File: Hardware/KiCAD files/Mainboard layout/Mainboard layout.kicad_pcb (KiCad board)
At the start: 2 copper layers, 87 parts, among them J1 Conn_01x02, J10 Conn_01x02, J14 Conn_01x03, J15 Conn_01x03, J2 Conn_01x06, J28 Conn_01x03, J3 Conn_01x02, J31 JST_03, J33 Conn_01x04, J34 JST_03, J35 JST_03, J36 JST_03, J37 JST_03, J38 JST_03, J39 JST_03, J4 Conn_01x06, J5 Conn_01x04, J6 Conn_01x06, J7 Conn_01x06, J8 Conn_01x06, J9 Conn_01x10, Q2 2DD1664, Q4 2N7000, SW8 Push_Button, SW9 Push_Button, U12 ESP32-S3-WROOM-1, U3 PCA9534PW

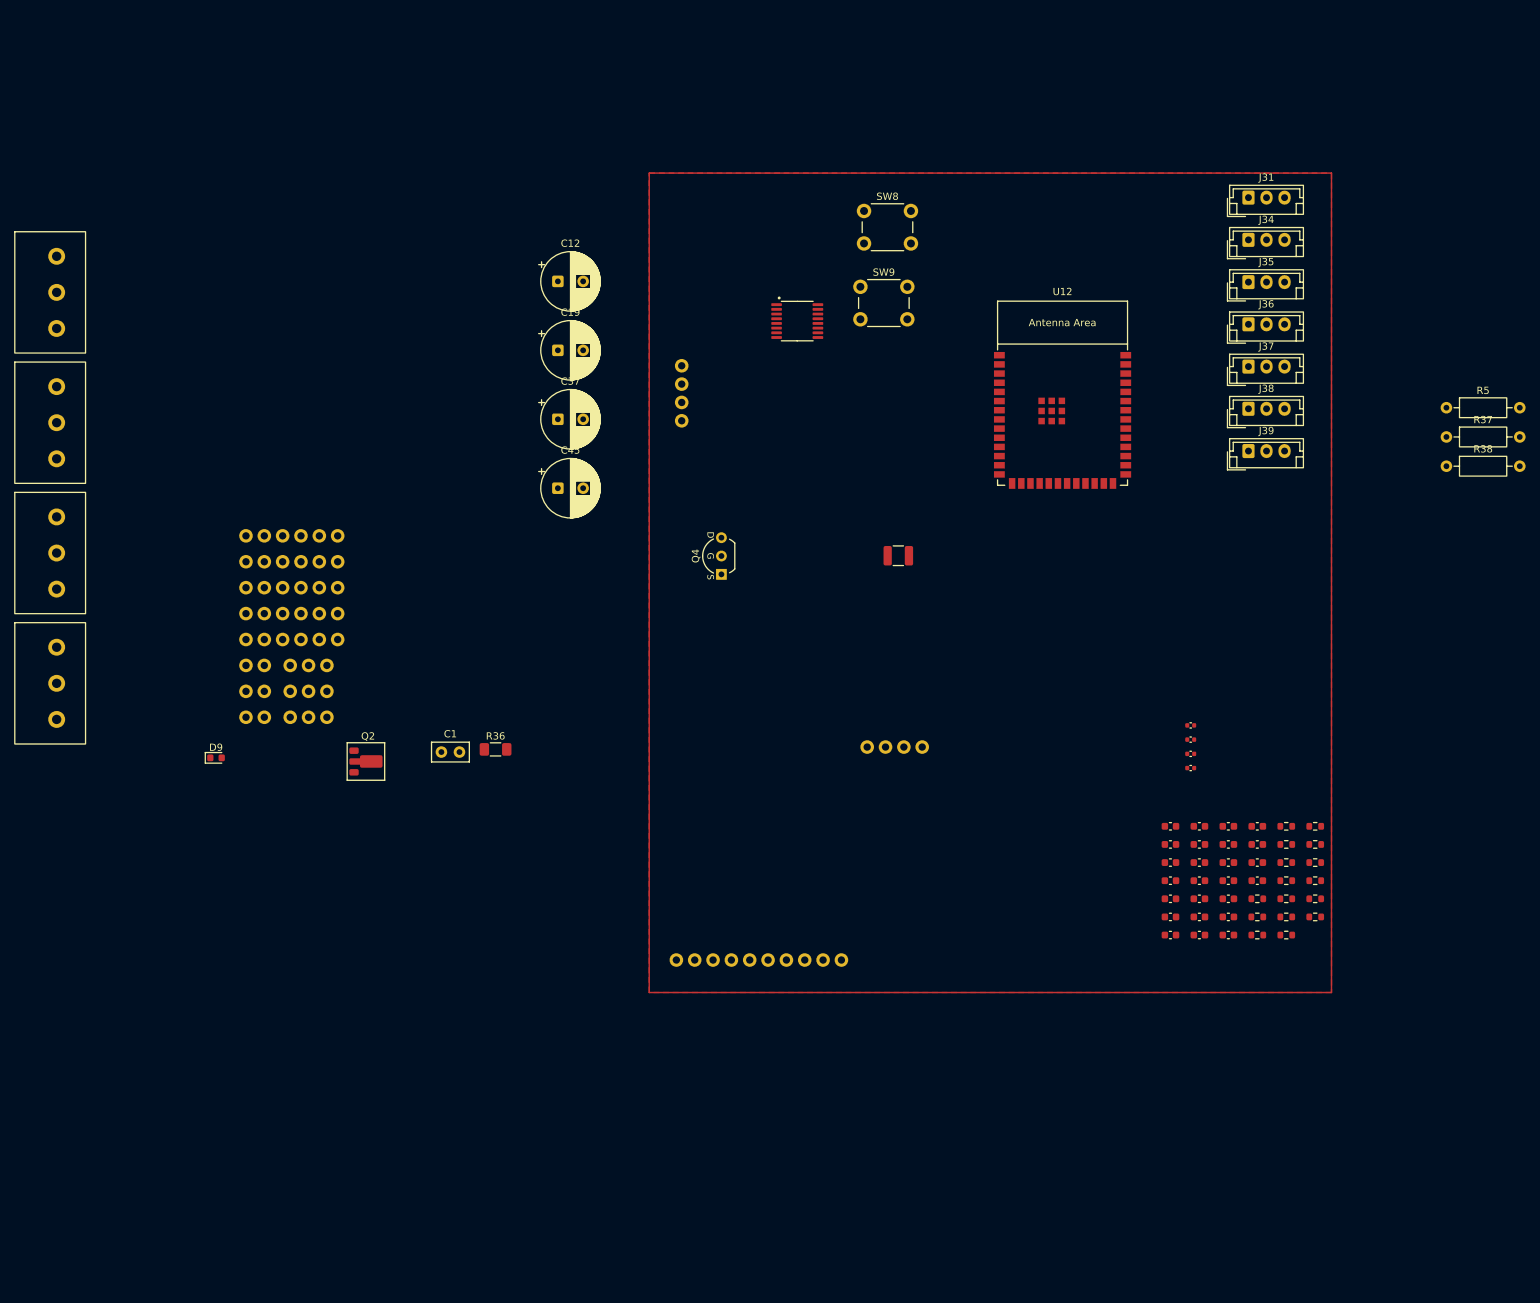
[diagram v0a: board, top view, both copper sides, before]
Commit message: Mainboard Layout V1
completed Mainboard V1 layout and one swapping side, a hotfix to come of the other board to take swapping side
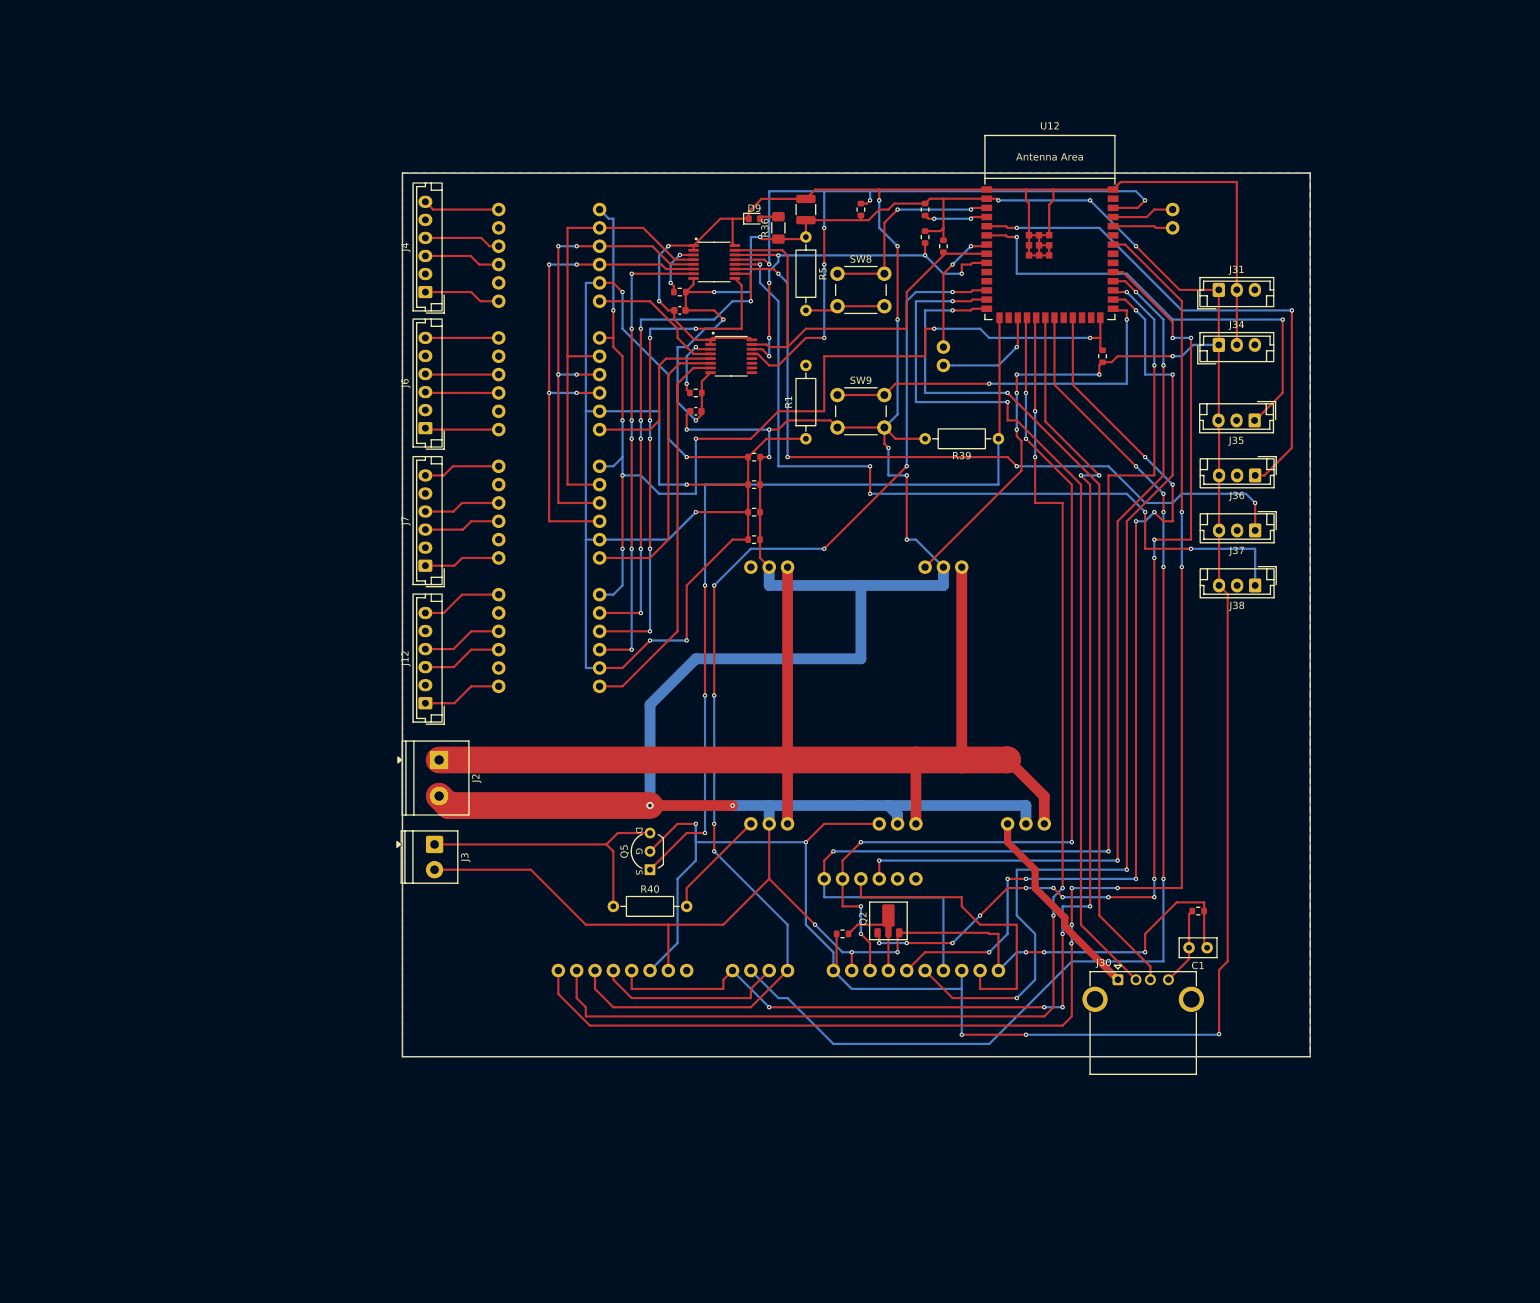
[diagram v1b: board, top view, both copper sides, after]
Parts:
- removed C10, C11, C13, C14, C15, C22, C29, C31, C32, C35, C36, C39, C40, C43, C44, C9: 0.1uF, PCM_SparkFun-Capacitor:C_0603_1608Metric
- removed C12, C19, C37, C45: 100uF_50V, Capacitor_THT:CP_Radial_D8.0mm_P3.50mm
- removed C17, C18, C30, C38: 4.7uF, PCM_SparkFun-Capacitor:C_0603_1608Metric
- removed C20, C27, C33, C41: 470nF, PCM_SparkFun-Capacitor:C_0402_1005Metric
- removed C21, C28, C34, C42: 10nF, PCM_SparkFun-Capacitor:C_0603_1608Metric
- removed J33: Conn_01x04, PCM_SparkFun-Connector:1x04_P2.54mm
- removed J39: JST_03, Connector_JST:JST_EH_B3B-EH-A_1x03_P2.50mm_Vertical
- removed Q4: 2N7000, PCM_Package_TO_SOT_THT_AKL:TO-92_Inline_Wide_SGD
- removed R10, R19, R24, R29: 1.5k, PCM_SparkFun-Resistor:R_0603_1608Metric
- removed R11, R21, R26, R31: 10k Linear, PCM_SparkFun-Resistor:Bourns-PDB18
- removed R12, R22, R27, R32: 10k, PCM_SparkFun-Resistor:R_0603_1608Metric
- removed R37, R38: 10k, Resistor_THT:R_Axial_DIN0207_L6.3mm_D2.5mm_P10.16mm_Horizontal
- added C23: 0.1uF, PCM_SparkFun-Capacitor:C_0603_1608Metric, F.Cu at (124.5, 47.0)
- added J11: Conn_01x06, PCM_SparkFun-Connector:1x06_P2.54mm, F.Cu at (97.2, 31.8)
- added J12: JST_06, Connector_JST:JST_EH_B6B-EH-A_1x06_P2.50mm_Vertical, F.Cu at (87.0, 87.4)
- added J13: Conn_01x08, PCM_SparkFun-Connector:1x08_P2.54mm, F.Cu at (123.2, 124.5)
- added J17: Conn_01x06, PCM_SparkFun-Connector:1x06_P2.54mm, F.Cu at (97.2, 49.5)
- added J19: Conn_01x06, PCM_SparkFun-Connector:1x06_P2.54mm, F.Cu at (97.2, 67.3)
- added J21: Conn_01x06, PCM_SparkFun-Connector:1x06_P2.54mm, F.Cu at (97.2, 85.1)
- added J22: Conn_01x03, PCM_SparkFun-Connector:1x03_P2.54mm, F.Cu at (156.2, 68.6)
- added J23: Conn_01x06, PCM_SparkFun-Connector:1x06_P2.54mm, F.Cu at (111.1, 31.8)
- added J24: Conn_01x06, PCM_SparkFun-Connector:1x06_P2.54mm, F.Cu at (111.1, 49.5)
- added J25: Conn_01x06, PCM_SparkFun-Connector:1x06_P2.54mm, F.Cu at (111.1, 67.3)
- added J26: Conn_01x06, PCM_SparkFun-Connector:1x06_P2.54mm, F.Cu at (111.1, 85.1)
- added J29: Conn_01x03, PCM_SparkFun-Connector:1x03_P2.54mm, F.Cu at (132.1, 68.6)
- added J30: USB-A1VSB6, Connector_USB:USB_A_Kycon_KUSBX-AS1N-B_Horizontal, F.Cu at (182.9, 125.7)
- added Q5: 2N7000, PCM_Package_TO_SOT_THT_AKL:TO-92_Inline_Wide_SGD, F.Cu at (118.1, 110.5)
- added R1: 1k, Resistor_THT:R_Axial_DIN0207_L6.3mm_D2.5mm_P10.16mm_Horizontal, F.Cu at (139.7, 50.8)
- added R107: 4K7, PCM_SparkFun-Resistor:R_0603_1608Metric, F.Cu at (132.5, 64.8)
- added R39: 10k, Resistor_THT:R_Axial_DIN0207_L6.3mm_D2.5mm_P10.16mm_Horizontal, F.Cu at (166.4, 50.8)
- added R40: 100k, Resistor_THT:R_Axial_DIN0207_L6.3mm_D2.5mm_P10.16mm_Horizontal, F.Cu at (113.0, 115.6)
- added R54: 10k, PCM_SparkFun-Resistor:R_0603_1608Metric, F.Cu at (124.5, 44.5)
- added R89: 4K7, PCM_SparkFun-Resistor:R_0603_1608Metric, F.Cu at (132.5, 53.3)
- added R90: 4K7, PCM_SparkFun-Resistor:R_0603_1608Metric, F.Cu at (132.5, 57.1)
- added R91: 4K7, PCM_SparkFun-Resistor:R_0603_1608Metric, F.Cu at (132.5, 61.0)
- added U5: PCA9534PW, PCM_SparkFun-Semiconductor-Standard:TSSOP-16_4.4x5mm_P0.65mm, F.Cu at (129.4, 39.4)
- J1: value Conn_01x02 -> Programmer pins Conn_01x02
- J2: value Conn_01x06 -> Screw_Terminal_2_P5.00mm; footprint PCM_SparkFun-Connector:1x06_P2.54mm -> TerminalBlock_Phoenix:TerminalBlock_Phoenix_PT-1,5-2-5.0-H_1x02_P5.00mm_Horizontal
- J3: value Conn_01x02 -> Screw_Terminal_2_P3.50mm; footprint PCM_SparkFun-Connector:1x02_P2.54mm -> TerminalBlock_Phoenix:TerminalBlock_Phoenix_PT-1,5-2-3.5-H_1x02_P3.50mm_Horizontal
- J4, J6, J7: value Conn_01x06 -> JST_06; footprint PCM_SparkFun-Connector:1x06_P2.54mm -> Connector_JST:JST_EH_B6B-EH-A_1x06_P2.50mm_Vertical
- moved J1 143.0 mm to (190.5, 19.1), turned to -90 degrees
- moved R51 118.3 mm to (122.2, 30.5), turned to 180 degrees
- moved R55 116.4 mm to (147.3, 19.1), turned to 90 degrees
- moved C16 110.0 mm to (122.2, 33.0), turned to 180 degrees
- moved C1 109.5 mm to (195.3, 121.3), turned to 180 degrees
- moved J10 109.4 mm to (158.8, 38.1), turned to -90 degrees
- moved D9 105.5 mm to (132.6, 20.3)
- moved R52 104.2 mm to (156.2, 22.9), turned to 90 degrees
- moved R53 104.0 mm to (158.8, 24.1), turned to 90 degrees
- moved R50 103.2 mm to (156.2, 19.1), turned to 90 degrees
- moved J28 100.5 mm to (167.6, 104.1)
- moved R5 91.8 mm to (139.7, 22.9), turned to -90 degrees
- moved J8 86.7 mm to (142.2, 111.8)
- moved J15 83.6 mm to (149.9, 104.1)
- moved R36 82.2 mm to (135.9, 21.6), turned to 90 degrees
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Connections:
- net Net-(J1-Pin_1) renamed /TX
- net Net-(J1-Pin_2) renamed /RX
- C1 pad 1: 3.3V_in1 -> GND
- C16 pad 2: 3.3V_in1 -> GND
- C2 pad 2: 3.3V_in1 -> GND
- D9 pad 1: 3.3V_in1 -> GND
- J14 pad 2: 3.3V_in1 -> GND
- J15 pad 2: 3.3V_in1 -> GND
- J2 pad 1: /B2 -> +24V
- J2 pad 2: unconnected-(J2-Pin_2-Pad2) -> GND
- J28 pad 2: 3.3V_in1 -> GND
- J3 pad 1: TEMP_HOTPLATE -> SSR_Switch
- J3 pad 2: 3.3V_in1 -> GND
- J31 pad 2: 3.3V_in1 -> GND
- J34 pad 2: 3.3V_in1 -> GND
- J4 pad 1: /B2 -> B2_DRV0
- J4 pad 3: /A2 -> A2_DRV0
- J4 pad 4: /B1 -> B1_DRV0
- J4 pad 6: /A1 -> A1_DRV0
- J5 pad 2: MISO_1 -> CHAINL0_MISO_1
- J6 pad 1: /B2 -> B2_DRV1
- J6 pad 3: /A2 -> A2_DRV1
- J6 pad 4: /B1 -> B1_DRV1
- J6 pad 6: /A1 -> A1_DRV1
- J7 pad 1: /B2 -> B2_DRV2
- J7 pad 3: /A2 -> A2_DRV2
- J7 pad 4: /B1 -> B1_DRV2
- J7 pad 6: /A1 -> A1_DRV2
- J8 pad 1: SPI4_SCK -> SPI4_CLK
- J9 pad 10: 3.3V_in1 -> GND
- J9 pad 2: 3.3V_in1 -> GND
- Q2 pad 3: 3.3V_in1 -> GND
- R6 pad 1: 3.3V_in1 -> GND
- SW9 pad 2: 3.3V_in1 -> GND
- U12 pad 1: 3.3V_in1 -> GND
- U12 pad 10: Net-(J33-Pin_1) -> unconnected-(U12-GPIO17/U1TXD/ADC2_CH6-Pad10)
- U12 pad 11: Net-(J33-Pin_2) -> unconnected-(U12-GPIO18/U1RXD/ADC2_CH7/CLK_OUT3-Pad11)
- U12 pad 16: DIR -> unconnected-(U12-GPIO46-Pad16)
- U12 pad 34: unconnected-(U12-MTDI/GPIO41/CLK_OUT1-Pad34) -> DRDY_ALOW
- U12 pad 35: unconnected-(U12-MTMS/GPIO42-Pad35) -> TFT_interrupt
- U12 pad 39: TEMP_HOTPLATE -> unconnected-(U12-GPIO1/TOUCH1/ADC1_CH0-Pad39)
- U12 pad 40: 3.3V_in1 -> GND
- U12 pad 41: 3.3V_in1 -> GND
- U3 pad 1: 3.3V_in1 -> GND
- U3 pad 16: 3.3V_in1 -> GND
- U3 pad 2: 3.3V_in1 -> GND
- U3 pad 4: MODE_2_GPIO -> MODE_0_GPIO
- U3 pad 6: MODE_0_GPIO -> MODE_2_GPIO
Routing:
- net GND: track 0.00 -> 607.6 mm, vias 0 -> 19
- net +3.3V: track 0.00 -> 452.2 mm, vias 0 -> 17
- net DRIVER_0_STEP: track 0.00 -> 205.5 mm, vias 0 -> 6
- net DRDY_ALOW: track 0.00 -> 203.8 mm, vias 0 -> 6
- net MISO_1: track 0.00 -> 172.1 mm, vias 0 -> 4
- net SPI1_CLK: track 0.00 -> 171.6 mm, vias 0 -> 7
- net MOSI_1: track 0.00 -> 161.5 mm, vias 0 -> 5
- net +24V: track 0.00 -> 160.9 mm
- net SPI4_CLK: track 0.00 -> 159.0 mm, vias 0 -> 4
- net SPI1_CS: track 0.00 -> 158.0 mm, vias 0 -> 7
- net N_ENBL: track 0.00 -> 156.1 mm, vias 0 -> 7
- net Net-(Q2-B): track 0.00 -> 141.7 mm, vias 0 -> 14
- net MOSI_4: track 0.00 -> 137.6 mm, vias 0 -> 4
- net DATA_SELECT: track 0.00 -> 131.1 mm, vias 0 -> 8
- net SPI4_CS: track 0.00 -> 126.4 mm, vias 0 -> 6
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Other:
- board outline added: 125.7 x 122.4 mm
